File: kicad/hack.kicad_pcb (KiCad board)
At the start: 2 copper layers, 33.9 x 24.1 mm, 34 parts, among them P1 USB_micro, P2 CONN_01X13, P3 CONN_01X13, P4 CONN_01X01, U1 MIC5528, U2 STF202, U3 ATSAMD21E, X1 ABS07

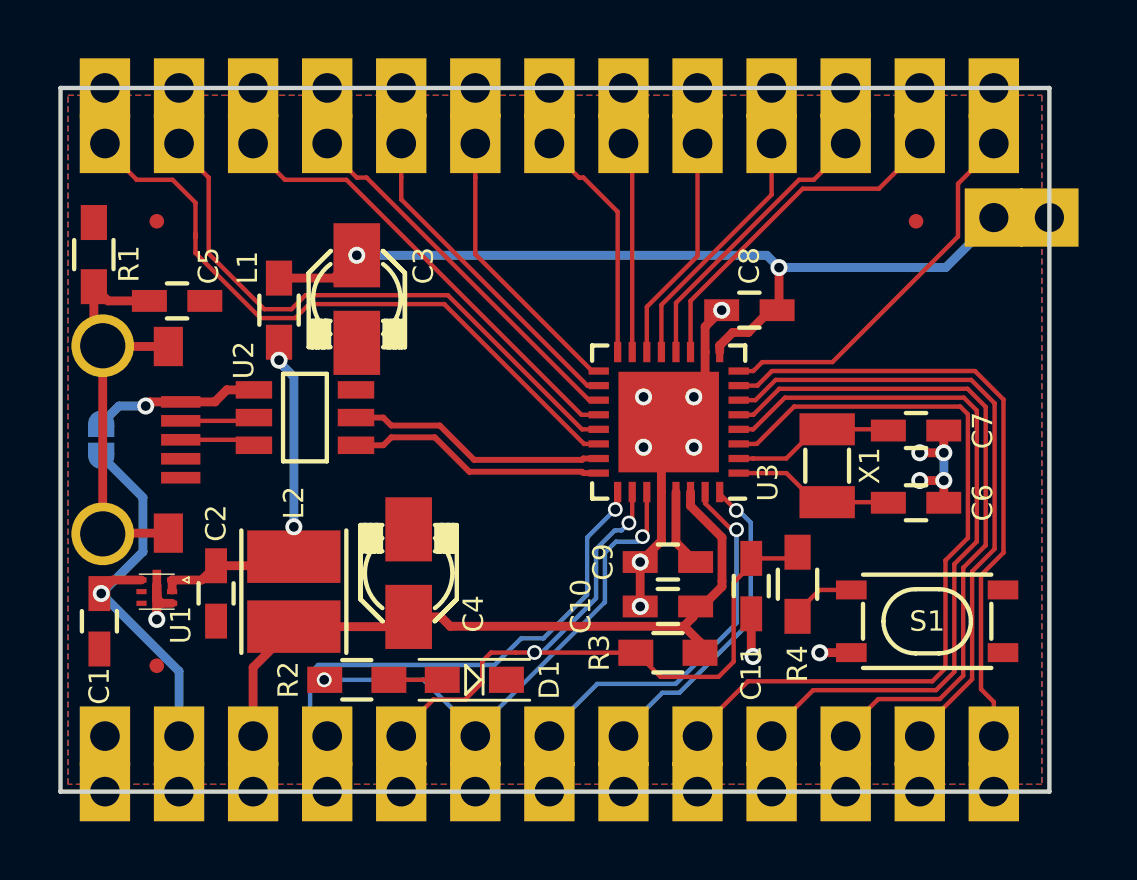
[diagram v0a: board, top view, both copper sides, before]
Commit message: added 3d model for ELL-VFG and some other minor edits
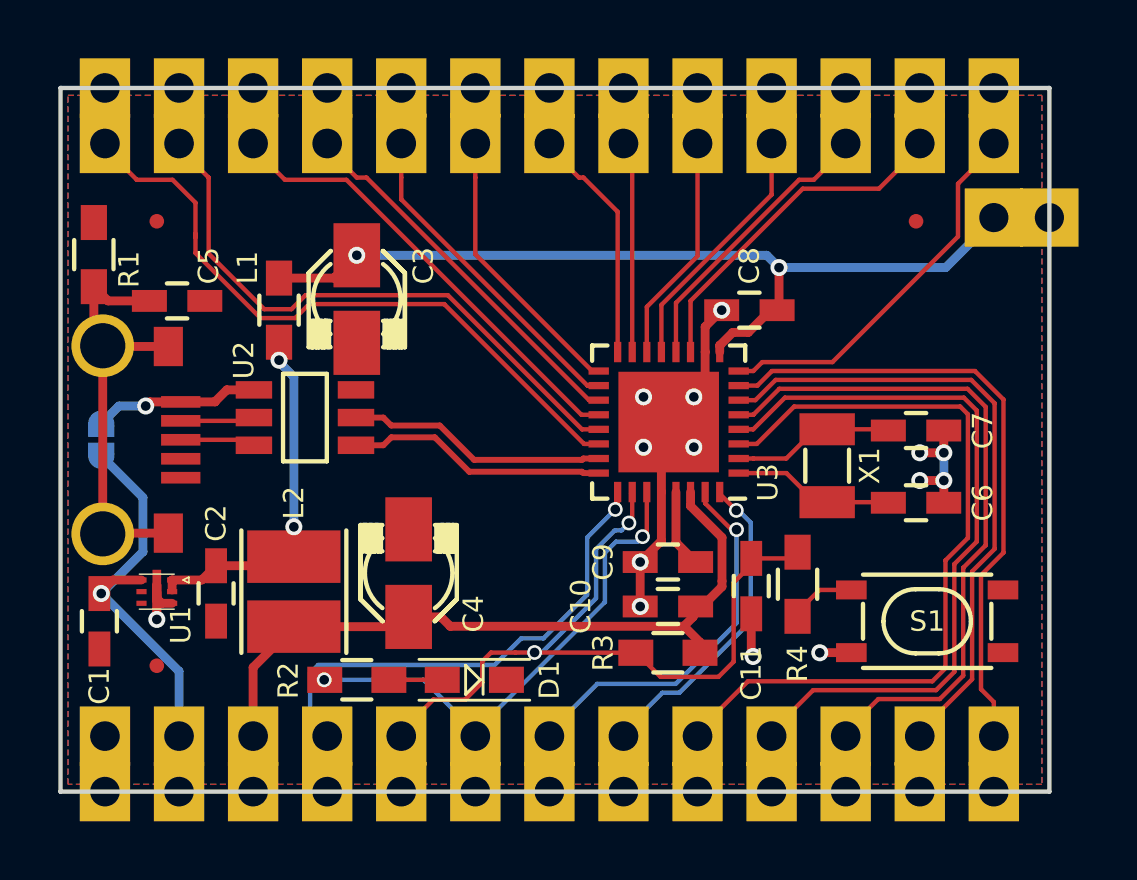
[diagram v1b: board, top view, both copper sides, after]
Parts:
- C1, C2: value 2.2u -> 2.2uF; footprint Capacitors_SMD:C_0603_HandSoldering -> hack-footprints:C_0603_HandSoldering
- C10, C11, C8, C9: value 100n -> 100nF; footprint Capacitors_SMD:C_0603_HandSoldering -> hack-footprints:C_0603_HandSoldering
- C3: value 10u -> 10uF; footprint c_elec_3x5.3 -> hack-footprints:c_elec_3x5.3
- C4: value 10u -> 10uF
- C5: value 4.5n -> 4.7nF; footprint Capacitors_SMD:C_0603_HandSoldering -> hack-footprints:C_0603_HandSoldering
- C6, C7: value 10p -> 10pF; footprint Capacitors_SMD:C_0603_HandSoldering -> hack-footprints:C_0603_HandSoldering
- D1: value BLUE -> RED
- FID3: footprint FIDUCIAL -> hack-footprints:FIDUCIAL
- L2: value 10u -> 10uH; footprint ELLVFG -> hack-footprints:ELLVFG
- P4: footprint Pin_Castellated_1x01 -> hack-footprints:Pin_Castellated_1x01
- R1, R4: footprint Resistors_SMD:R_0603_HandSoldering -> hack-footprints:R_0603_HandSoldering
- R2: value 68 -> 330; footprint Resistors_SMD:R_0603_HandSoldering -> hack-footprints:R_0603_HandSoldering
- R3: value 10K -> 10k; footprint Resistors_SMD:R_0603_HandSoldering -> hack-footprints:R_0603_HandSoldering
- S1: value SPST-M -> RST
- U3: footprint QFN-32-1EP_5x5mm_Pitch0.5mm -> hack-footprints:QFN-32-1EP_5x5mm_Pitch0.5mm
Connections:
- net VDDCORE renamed /VDDCORE
- net shield renamed /shield
- P1 pad 4: Net-(P1-Pad4) -> (no net)
- S1 pad 2: Net-(S1-Pad2) -> (no net)
- S1 pad 4: Net-(S1-Pad4) -> (no net)
- U1 pad 4: Net-(U1-Pad4) -> (no net)
- U1 pad 5: Net-(U1-Pad5) -> (no net)

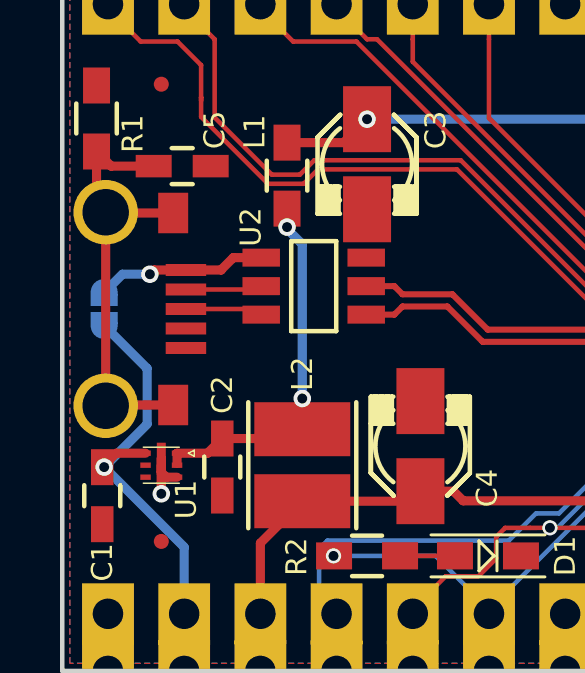
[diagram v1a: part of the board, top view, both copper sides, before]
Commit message: Added secondary USB connector footprint
Previous one is only available from Seeedstudio, this one is from FCI
and available from all distributors
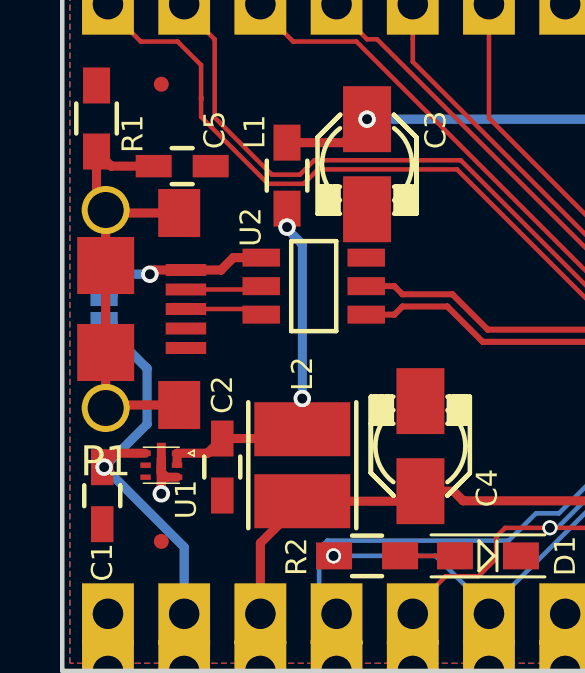
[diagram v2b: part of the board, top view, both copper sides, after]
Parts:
- P1: footprint hack-footprints:ST-USB-001G -> 10118193-0001LF
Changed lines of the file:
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@@
-(kicad_pcb (version 4) (host pcbnew 4.0.1-3.201512202202+6198~38~ubuntu15.04.1-stable)
+(kicad_pcb (version 4) (host pcbnew "(2015-08-16 BZR 6097, Git b384c94)-product")
   (general
-    (links 114)
+    (links 116)
     (no_connects 0)
-    (area 153.340999 74.219999 187.400001 98.500001)
+    (area 146.007619 68.952 197.019383 100.352401)
     (thickness 1.6)
     (drawings 47)
-    (tracks 380)
+    (tracks 381)
     (zones 0)
     (modules 34)
@@
     (add_net !RESET)
     (add_net /VDDCORE)
-    (add_net /shield)
     (add_net "Net-(D1-Pad1)")
     (add_net "Net-(P1-Pad2)")
@@
     (uvia_dia 0.3556)
     (uvia_drill 0.254)
+    (add_net /shield)
     (add_net GND)
     (add_net VBUS)
@@
     (add_net USB-D+)
     (add_net USB-D-)
+  )
+  (module 10118193-0001LF (layer F.Cu)
+    (at 154.8638 86.36)
+    (fp_text reference P1 (at 0 5.08) (layer F.SilkS)
+      (effects (font (size 1 1) (thickness 0.15)))
+    )
+    (fp_text value USB_micro (at 0 -5.08) (layer F.Fab)
+      (effects (font (size 1 1) (thickness 0.15)))
+    )
+    (fp_line (start 3.6 3.7) (end -1.45 3.7) (layer F.CrtYd) (width 0.15))
+    (fp_line (start 3.6 -3.7) (end 3.6 3.7) (layer F.CrtYd) (width 0.15))
+    (fp_line (start -1.45 -3.7) (end 3.6 -3.7) (layer F.CrtYd) (width 0.15))
+    (fp_line (start -1.45 -3.7) (end -1.45 3.7) (layer F.CrtYd) (width 0.15))
+    (pad 1 smd rect (at 2.675 -1.3) (size 1.35 0.4) (layers F.Cu F.Paste F.Mask)
+      (net 13 VBUS) (solder_mask_margin 0.0762) (solder_paste_margin -0.0762) (clearance 0.0762))
+    (pad 2 smd rect (at 2.675 -0.65) (size 1.35 0.4) (layers F.Cu F.Paste F.Mask)
+      (net 5 "Net-(P1-Pad2)") (solder_mask_margin 0.0762) (solder_paste_margin -0.0762) (clearance 0.0762))
+    (pad 3 smd rect (at 2.675 0) (size 1.35 0.4) (layers F.Cu F.Paste F.Mask)
+      (net 6 "Net-(P1-Pad3)") (solder_mask_margin 0.0762) (solder_paste_margin -0.0762) (clearance 0.0762))
+    (pad 4 smd rect (at 2.675 0.65) (size 1.35 0.4) (layers F.Cu F.Paste F.Mask)
+      (solder_mask_margin 0.0762) (solder_paste_margin -0.0762) (clearance 0.0762))
+    (pad 5 smd rect (at 2.675 1.3) (size 1.35 0.4) (layers F.Cu F.Paste F.Mask)
+      (net 1 GND) (solder_mask_margin 0.0762) (solder_paste_margin -0.0762) (clearance 0.0762))
+    (pad 6 thru_hole circle (at 0 -3.3) (size 1.6 1.6) (drill 1.2) (layers *.Cu *.Mask)
+      (net 38 /shield) (solder_mask_margin 0.0762) (solder_paste_margin -0.0762) (clearance 0.0762))
+    (pad 6 thru_hole circle (at 0 3.3) (size 1.6 1.6) (drill 1.2) (layers *.Cu *.Mask)
+      (net 38 /shield) (solder_mask_margin 0.0762) (solder_paste_margin -0.0762) (clearance 0.0762))
+    (pad 6 smd rect (at 2.45 3.2) (size 1.4 1.6) (layers F.Cu F.Paste F.Mask)
+      (net 38 /shield) (solder_mask_margin 0.0762) (solder_paste_margin -0.0762) (clearance 0.0762))
+    (pad 6 smd rect (at 2.45 -3.2) (size 1.4 1.6) (layers F.Cu F.Paste F.Mask)
+      (net 38 /shield) (solder_mask_margin 0.0762) (clearance 0.0762))
+    (pad 6 smd rect (at 0 1.45) (size 1.9 1.9) (layers F.Cu F.Paste F.Mask)
+      (net 38 /shield) (solder_mask_margin 0.0762) (solder_paste_margin -0.0762) (clearance 0.0762))
+    (pad 6 smd rect (at 0 -1.45) (size 1.9 1.9) (layers F.Cu F.Paste F.Mask)
+      (net 38 /shield) (solder_mask_margin 0.0762) (solder_paste_margin -0.0762) (clearance 0.0762))
   )
   (module hack-footprints:Pin_Castellated_1x01 (layer B.Cu)
@@
     )
   )
-  (module hack-footprints:ST-USB-001G (layer F.Cu)
-    (at 154.8638 86.36)
-    (fp_text reference P1 (at -0.9398 0 270) (layer B.SilkS)
-      (effects (font (size 0.7 0.7) (thickness 0.1)) (justify mirror))
-    )
-    (fp_text value USB_micro (at -0.0508 0 90) (layer F.Fab)
-      (effects (font (size 0.7 0.7) (thickness 0.1)))
-    )
-    (fp_line (start 3.3 3.7) (end -1.45 3.7) (layer F.CrtYd) (width 0.15))
-    (fp_line (start 3.3 -3.7) (end 3.3 3.7) (layer F.CrtYd) (width 0.15))
-    (fp_line (start -1.45 -3.7) (end 3.3 -3.7) (layer F.CrtYd) (width 0.15))
-    (fp_line (start -1.45 -3.7) (end -1.45 3.7) (layer F.CrtYd) (width 0.15))
-    (pad 1 smd rect (at 2.675 -1.3) (size 1.35 0.4) (layers F.Cu F.Paste F.Mask)
-      (net 13 VBUS))
-    (pad 2 smd rect (at 2.675 -0.65) (size 1.35 0.4) (layers F.Cu F.Paste F.Mask)
-      (net 5 "Net-(P1-Pad2)"))
-    (pad 3 smd rect (at 2.675 0) (size 1.35 0.4) (layers F.Cu F.Paste F.Mask)
-      (net 6 "Net-(P1-Pad3)"))
-    (pad 4 smd rect (at 2.675 0.65) (size 1.35 0.4) (layers F.Cu F.Paste F.Mask))
-    (pad 5 smd rect (at 2.675 1.3) (size 1.35 0.4) (layers F.Cu F.Paste F.Mask)
-      (net 1 GND))
-    (pad 6 thru_hole circle (at 0 -3.225) (size 2.15 2.15) (drill 1.55) (layers *.Cu *.Mask)
-      (net 38 /shield))
-    (pad 6 thru_hole circle (at 0 3.225) (size 2.15 2.15) (drill 1.55) (layers *.Cu *.Mask)
-      (net 38 /shield))
-    (pad 6 smd rect (at 2.25 3.2) (size 1 1.35) (layers F.Cu F.Paste F.Mask)
-      (net 38 /shield))
-    (pad 6 smd rect (at 2.25 -3.2) (size 1 1.35) (layers F.Cu F.Paste F.Mask)
-      (net 38 /shield))
-    (model micro_USB-B_Molex_105017.wrl
-      (at (xyz 0 0 0))
-      (scale (xyz 1 1 1))
-      (rotate (xyz 0 0 0))
-    )
-  )
   (module hack-footprints:R_0603_HandSoldering (layer F.Cu)
     (at 154.559 80.01 270)
@@
   (via (at 172.439914 88.746914) (size 0.508) (drill 0.3302) (layers F.Cu B.Cu) (net 37))
   (segment (start 172.5205 88.1515) (end 172.5205 88.3765) (width 0.1524) (layer F.Cu) (net 37) (status 30))
-  (segment (start 154.8638 89.585) (end 154.8638 83.135) (width 0.3048) (layer F.Cu) (net 38))
+  (segment (start 154.8638 84.91) (end 154.8638 83.06) (width 0.3048) (layer F.Cu) (net 38))
+  (segment (start 154.8638 87.81) (end 154.8638 84.91) (width 0.3048) (layer F.Cu) (net 38))
+  (segment (start 154.8638 89.66) (end 154.8638 87.81) (width 0.3048) (layer F.Cu) (net 38))
   (segment (start 157.1138 89.56) (end 154.8888 89.56) (width 0.3048) (layer F.Cu) (net 38))
   (segment (start 154.8888 89.56) (end 154.8638 89.585) (width 0.3048) (layer F.Cu) (net 38))
@@
   (segment (start 154.559 82.8302) (end 154.8638 83.135) (width 0.3048) (layer F.Cu) (net 38))
   (segment (start 154.813 81.364) (end 154.559 81.11) (width 0.3048) (layer F.Cu) (net 38))
-  (segment (start 155.263 83.8975) (end 154.813 83.4475) (width 0.3048) (layer F.Cu) (net 38) (status 30))
   (segment (start 174.5205 89.8775) (end 175.194 90.551) (width 0.3048) (layer F.Cu) (net 39) (status 20))
   (segment (start 175.223 90.551) (end 175.448 90.551) (width 0.3048) (layer F.Cu) (net 39) (status 30))
@@
     (min_thickness 0.254)
     (keepout (tracks allowed) (vias not_allowed) (copperpour not_allowed))
-    (fill (arc_segments 16) (thermal_gap 0.508) (thermal_bridge_width 0.508))
+    (fill yes (arc_segments 16) (thermal_gap 0.508) (thermal_bridge_width 0.508))
     (polygon
       (pts
@@
     (min_thickness 0.254)
     (keepout (tracks not_allowed) (vias not_allowed) (copperpour not_allowed))
-    (fill (arc_segments 16) (thermal_gap 0.508) (thermal_bridge_width 0.508))
+    (fill yes (arc_segments 16) (thermal_gap 0.508) (thermal_bridge_width 0.508))
     (polygon
       (pts

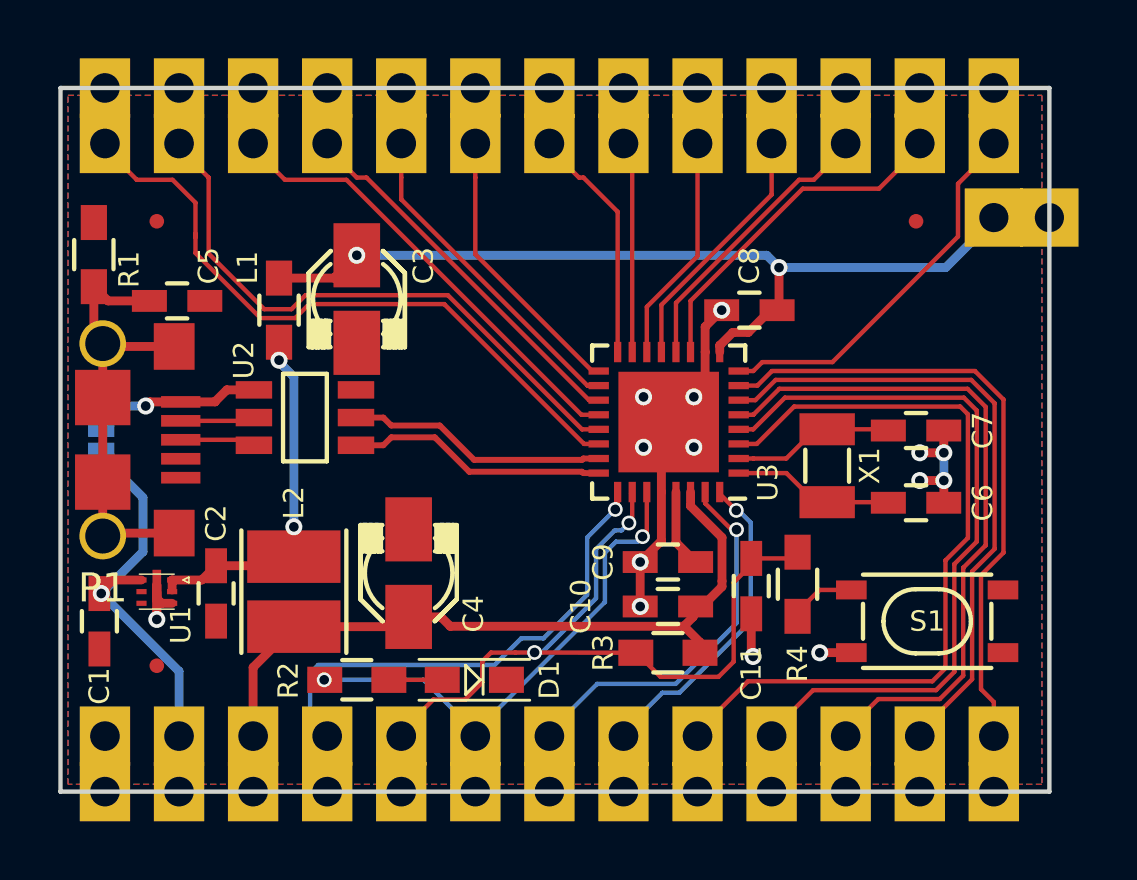
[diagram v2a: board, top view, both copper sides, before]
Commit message: Optimized footprints, freed some PCB real estate
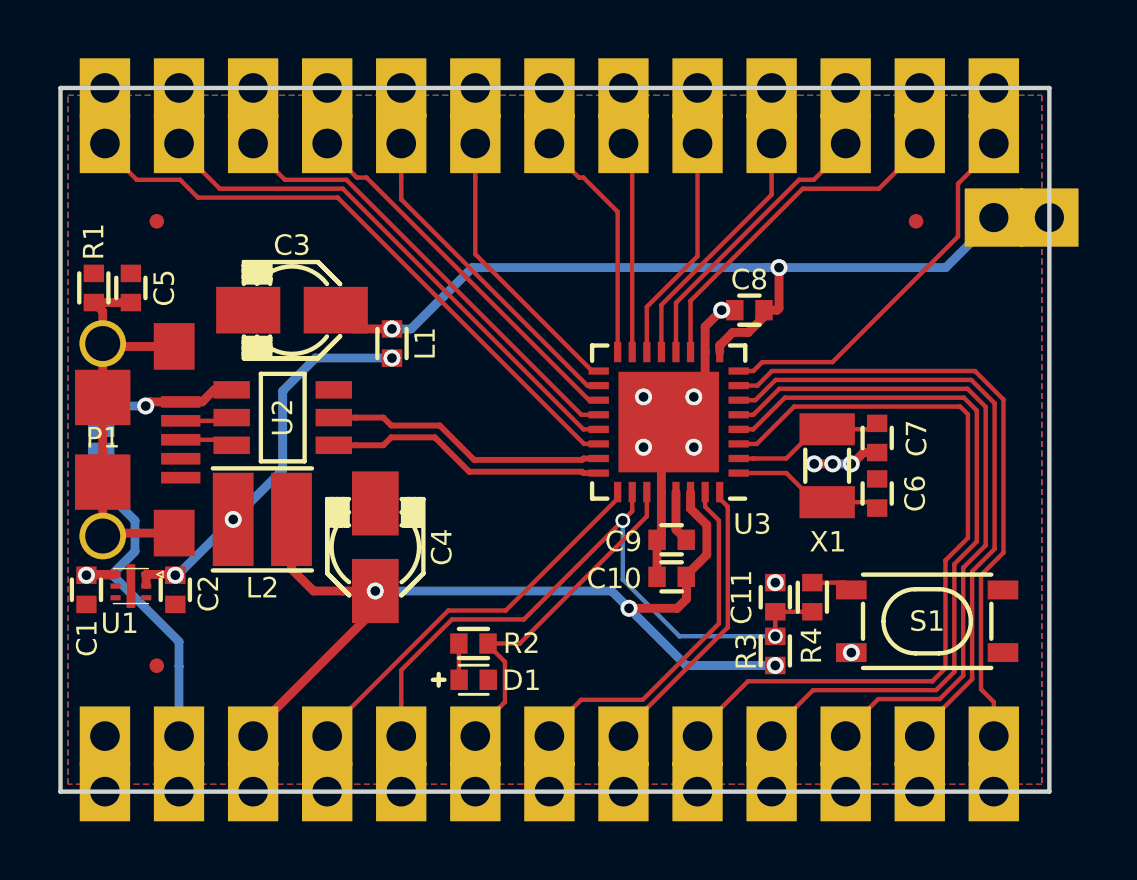
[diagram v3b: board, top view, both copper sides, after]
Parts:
- C1, C10, C11, C2, C5, C6, C7, C8, C9: footprint hack-footprints:C_0603_HandSoldering -> hack-footprints:C_0603
- D1: footprint hack-footprints:LED_0603_HandSoldering -> hack-footprints:LED_0603
- L1: footprint hack-footprints:L_0603_HandSoldering -> hack-footprints:L_0603
- R1, R2, R3, R4: footprint hack-footprints:R_0603_HandSoldering -> hack-footprints:R_0603
- S1: footprint hack-footprints:SPST-PTS_810 -> SPST-PTS_810
- U2: footprint hack-footprints:TSOP-6 -> TSOP-6
- X1: footprint hack-footprints:xtal_3.2x1.5mm -> xtal_3.2x1.5mm
- moved R2 4.19 mm to (167.6, 93.3), turned to 180 degrees
- moved L1 4.04 mm to (164.8, 83.1)
- moved R3 3.68 mm to (177.9, 93.6), turned to 270 degrees
- moved L2 2.70 mm to (160.3, 89.1), turned to 0 degrees
- moved C3 2.25 mm to (161.4, 81.9), turned to 90 degrees
- moved C5 1.65 mm to (155.8, 81.2), turned to 270 degrees
- moved C4 1.45 mm to (164.2, 90.0)
- moved C2 1.40 mm to (157.4, 91.5)
- moved C6 1.37 mm to (181.4, 88.2), turned to 90 degrees
- moved C7 1.36 mm to (181.4, 86.3), turned to 270 degrees
- moved C1 1.17 mm to (154.3, 91.5)
- moved R1 1.14 mm to (154.6, 81.2)
- moved C10 1.02 mm to (174.4, 91.1)
- moved C11 0.91 mm to (177.9, 91.8), turned to 90 degrees
- moved U1 0.91 mm to (155.8, 91.4)
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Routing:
- net GND: track 19.7 -> 11.5 mm, vias 14 -> 10
- net VDDF: track 27.0 -> 34.5 mm, vias 0 -> 3
- net PA28/13: track 19.1 -> 14.0 mm, vias 2 -> 0
- net PA27/12: track 19.1 -> 15.7 mm, vias 1 -> 0
- net !RESET: track 28.3 -> 25.4 mm
- net PA22/10: track 22.4 -> 20.4 mm
- net PA23/11: track 24.7 -> 23.2 mm
- net /shield: track 15.7 -> 14.4 mm
- net VDDANA: track 31.8 -> 30.5 mm
- net /VDDCORE: track 2.90 -> 1.78 mm
- net PA31/SWDIO: track 13.1 -> 12.1 mm, vias 1 -> 0
- net PA30/SWCLK: track 15.1 -> 14.1 mm, vias 1 -> 0
- net Net-(R4-Pad2): track 2.31 -> 1.44 mm
- net VBUS: track 5.72 -> 4.95 mm
- net USB-D-: track 8.94 -> 9.70 mm
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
